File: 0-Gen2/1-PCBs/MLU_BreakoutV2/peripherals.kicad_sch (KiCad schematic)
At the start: 88 parts, among them J10 430450228, J11 430450228, J12 430450228, J13 430450422, J14 430450228, J15 Conn_01x02_Socket, J16 430451027, J17 430450422, J18 PixHawk PM02, J19 Conn_01x04_Socket, J20 Conn_02x22_Odd_Even, J21 430450422, J22 Conn_01x03_Pin, J23 J1B1211CCD, J24 Conn_02x03_Odd_Even, J3 430450422, J4 430450422, J5 430450422, J6 Conn_01x02_Socket, J7 430450821, J8 430450228

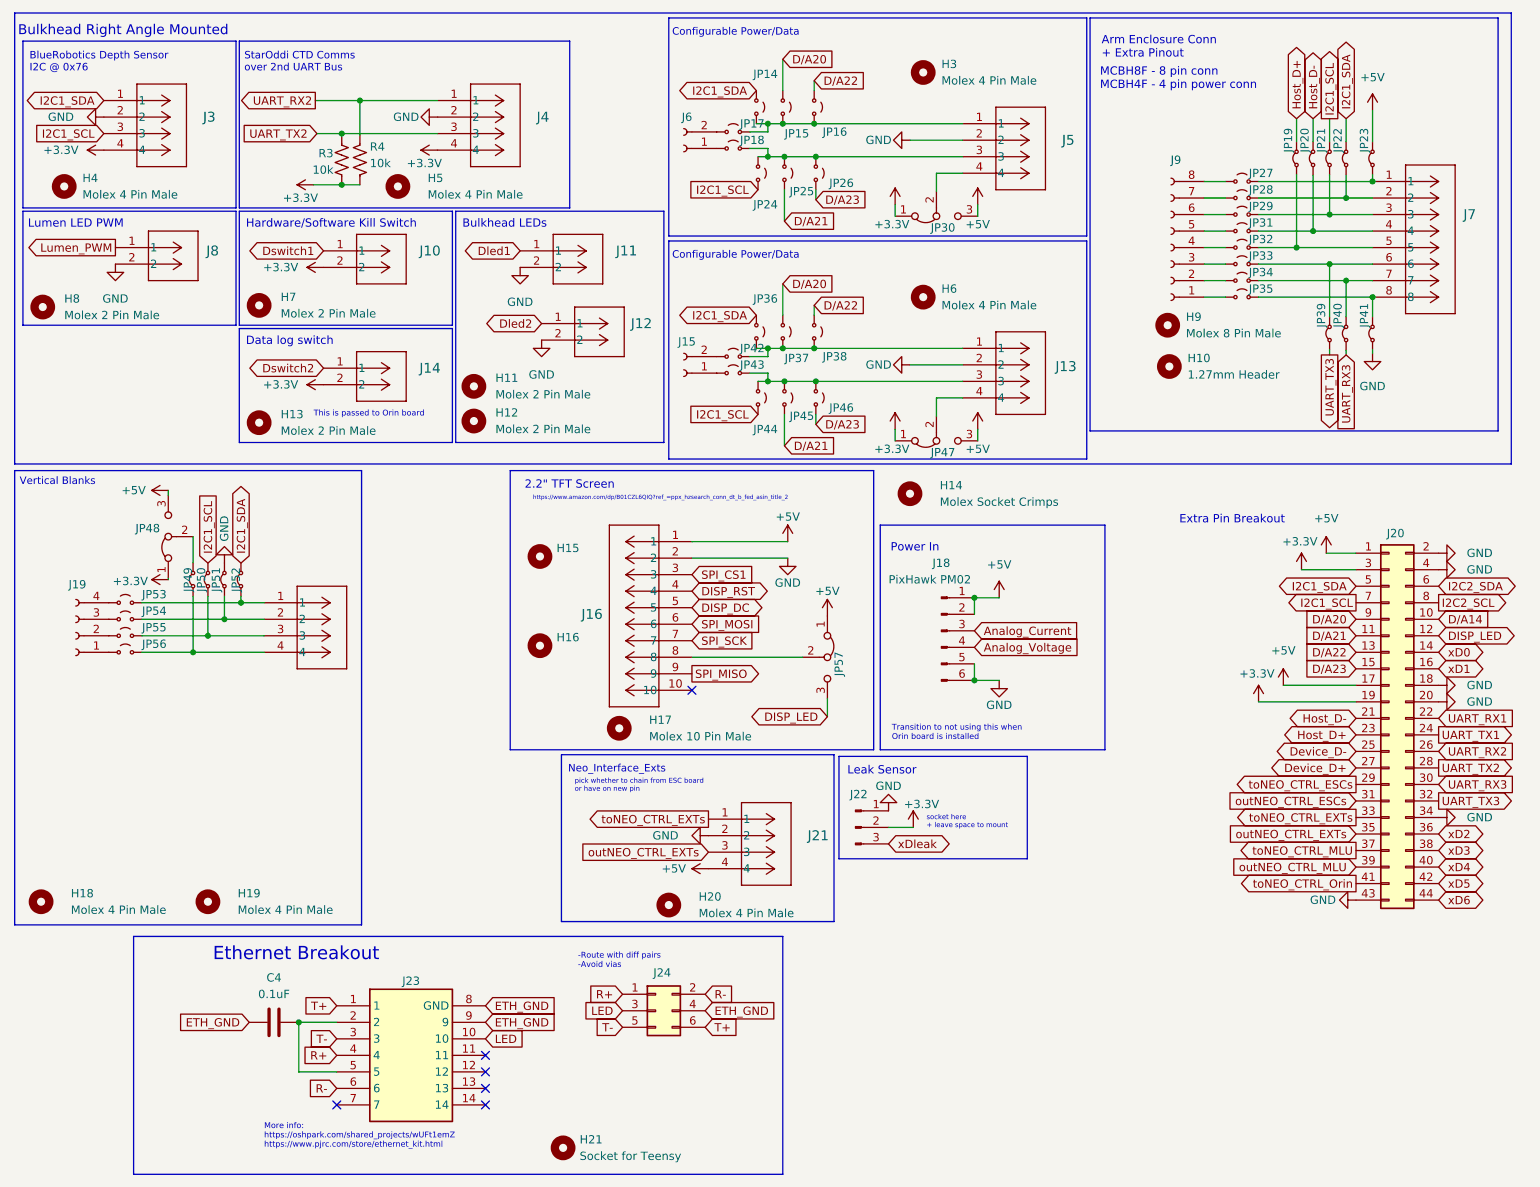
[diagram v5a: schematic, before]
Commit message: [bugfix] rescued footprints
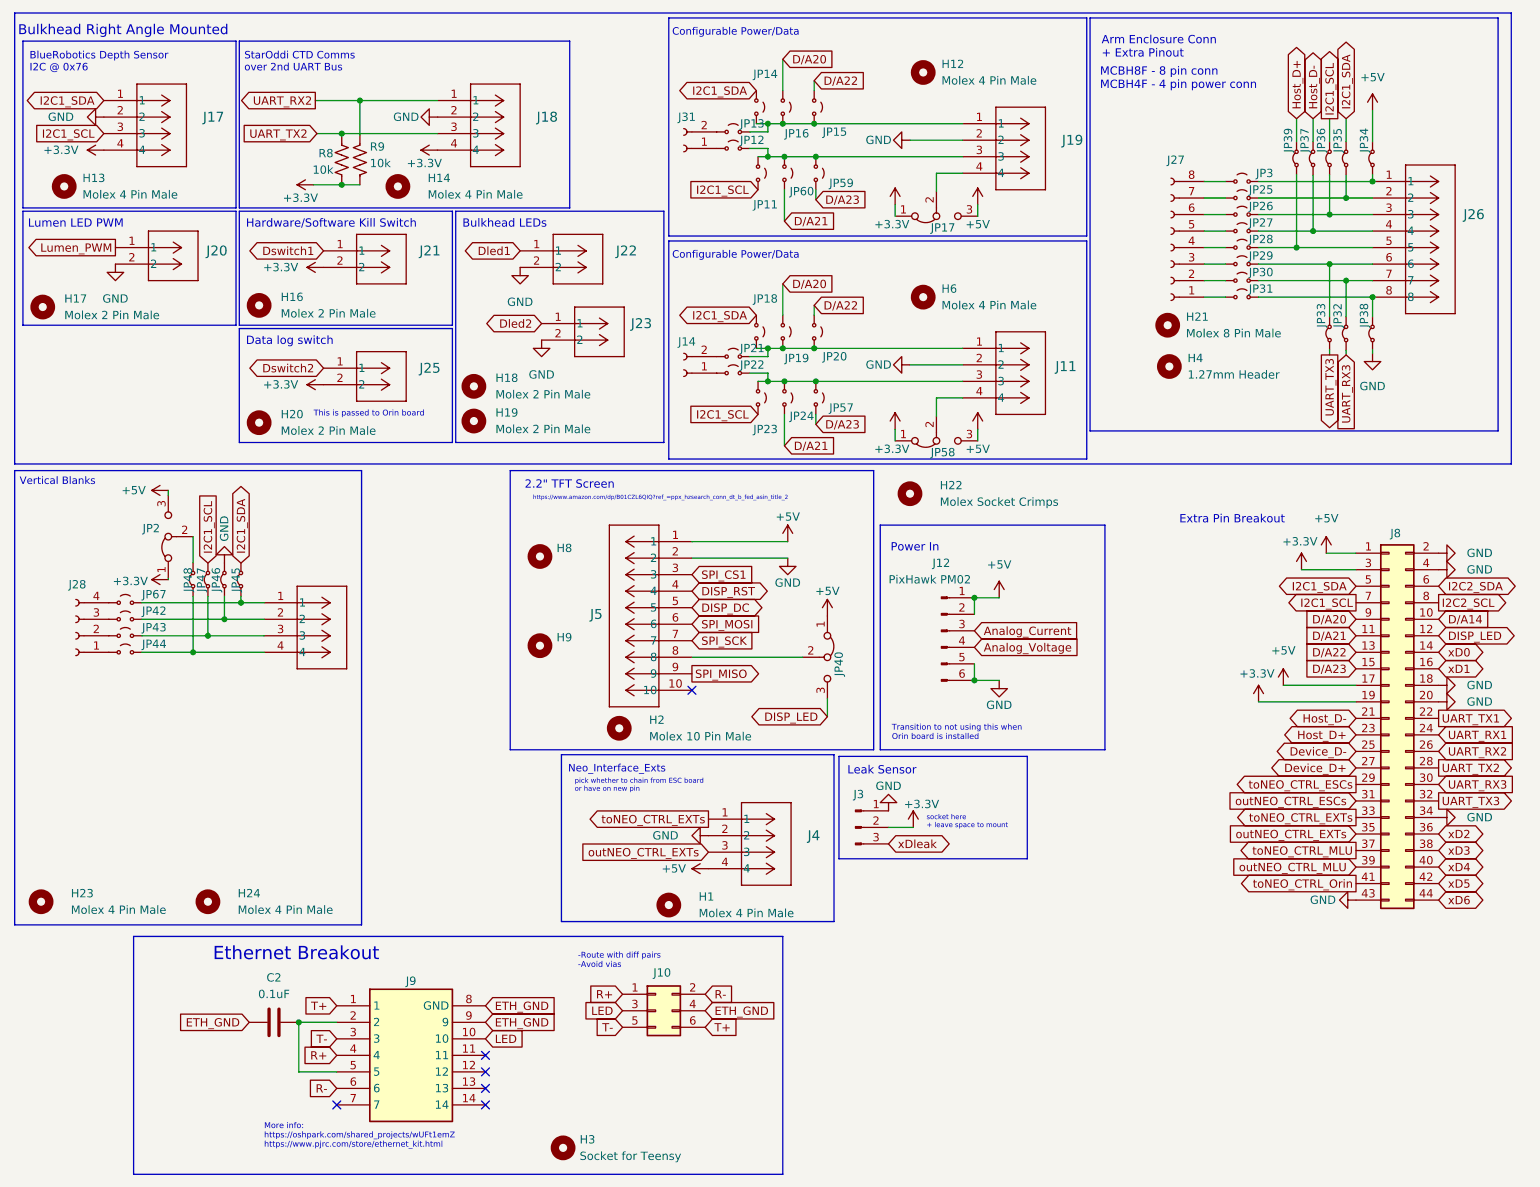
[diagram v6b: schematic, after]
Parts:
- renumbered C4 to C2, H20 to H1, H3 to H12, H4 to H13, H5 to H14, H7 to H16, H8 to H17, H11 to H18, H12 to H19, H17 to H2, H13 to H20, H9 to H21, H14 to H22, H18 to H23, H19 to H24, H21 to H3, H10 to H4, H15 to H8, H16 to H9, J24 to J10, J13 to J11, J18 to J12, J15 to J14, J3 to J17, J4 to J18, J5 to J19, J17 to J2, J8 to J20, J10 to J21, J11 to J22, J12 to J23, J14 to J25, J7 to J26, J9 to J27, J19 to J28, J22 to J3, J6 to J31, J21 to J4, J16 to J5, J20 to J8, J23 to J9, JP24 to JP11, JP18 to JP12, JP17 to JP13, JP16 to JP15, JP15 to JP16, JP30 to JP17, JP36 to JP18, JP37 to JP19, JP48 to JP2, JP38 to JP20, JP42 to JP21, JP43 to JP22, JP44 to JP23, JP45 to JP24, JP28 to JP25, JP29 to JP26, JP31 to JP27, JP32 to JP28, JP33 to JP29, JP27 to JP3, JP34 to JP30, JP35 to JP31, JP40 to JP32, JP39 to JP33, JP23 to JP34, JP22 to JP35, JP21 to JP36, JP20 to JP37, JP41 to JP38, JP19 to JP39, JP57 to JP40, JP54 to JP42, JP55 to JP43, JP56 to JP44, JP52 to JP45, JP51 to JP46, JP50 to JP47, JP49 to JP48, JP46 to JP57, JP47 to JP58, JP26 to JP59, JP25 to JP60, JP53 to JP67, R3 to R8, R4 to R9
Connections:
- net UART_RX1: now also J8.24 (Pin_24); no longer J8.22 (Pin_22)
- net UART_TX1: now also J8.22 (Pin_22); no longer J8.24 (Pin_24)
